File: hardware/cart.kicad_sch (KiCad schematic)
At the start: 4 parts, among them P1 MD-CART-FINGERS

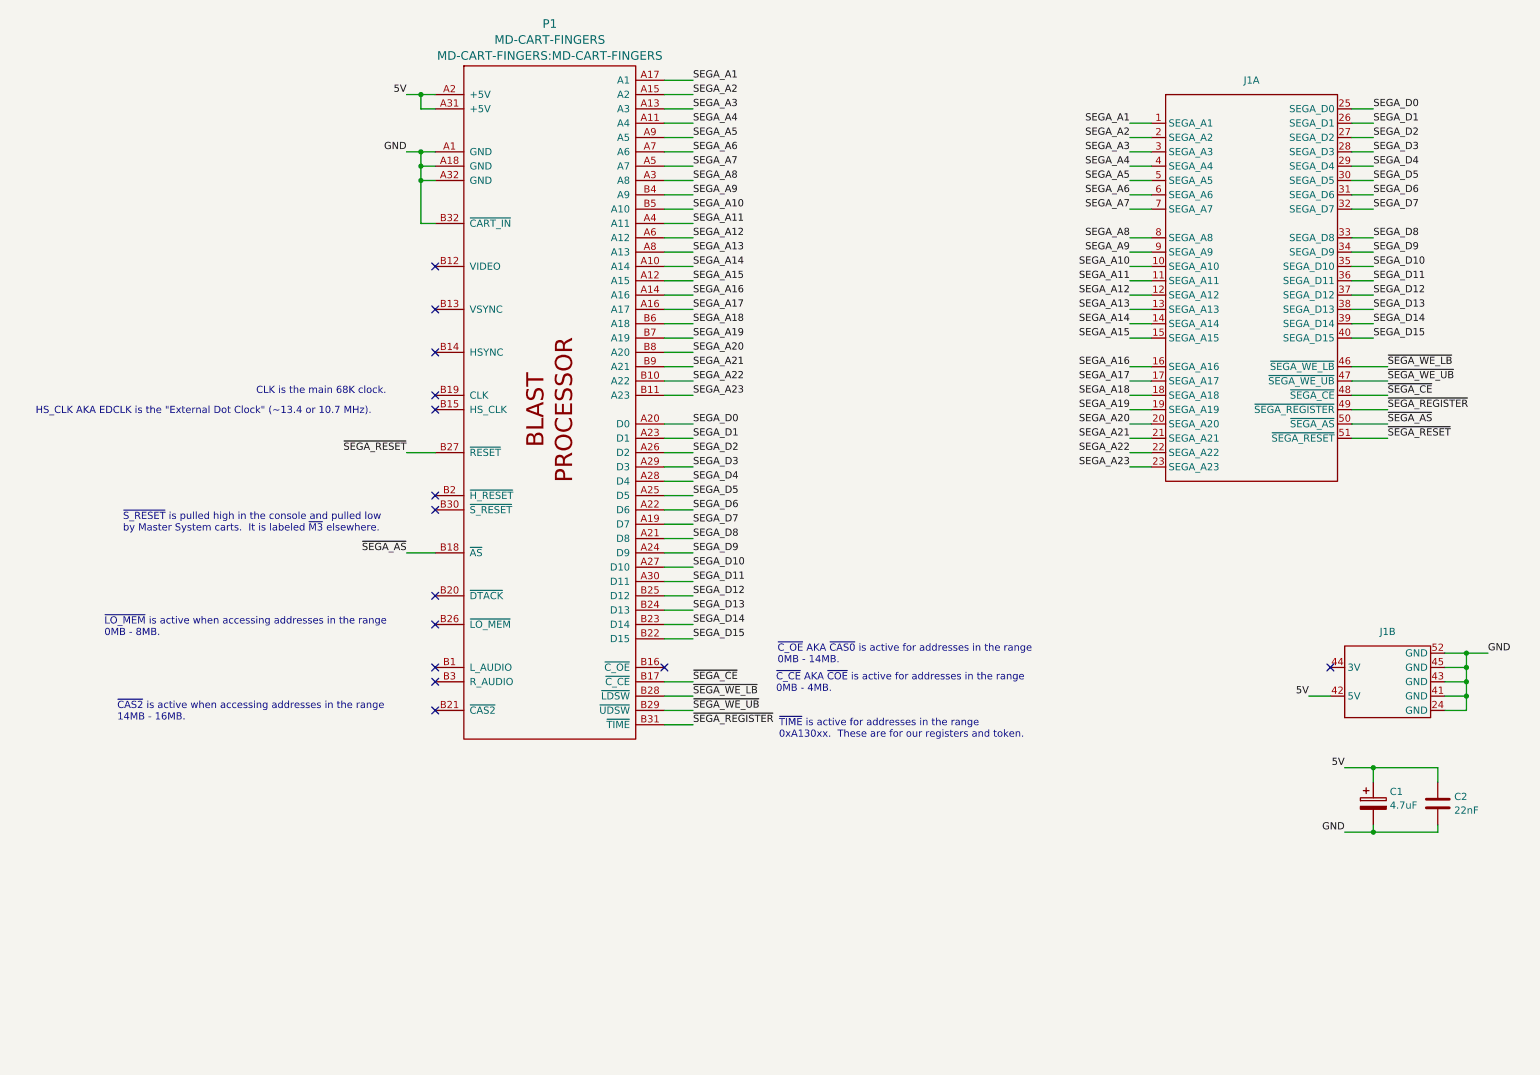
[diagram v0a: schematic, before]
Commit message: Massively reorganize board designs
Now planning to have most assembly done by JLCPCB, so trace sizes,
part selections, etc. are set accordingly.

New boards are:
 - cartridge interface & flash
 - microcontroller & registers
 - sram x2
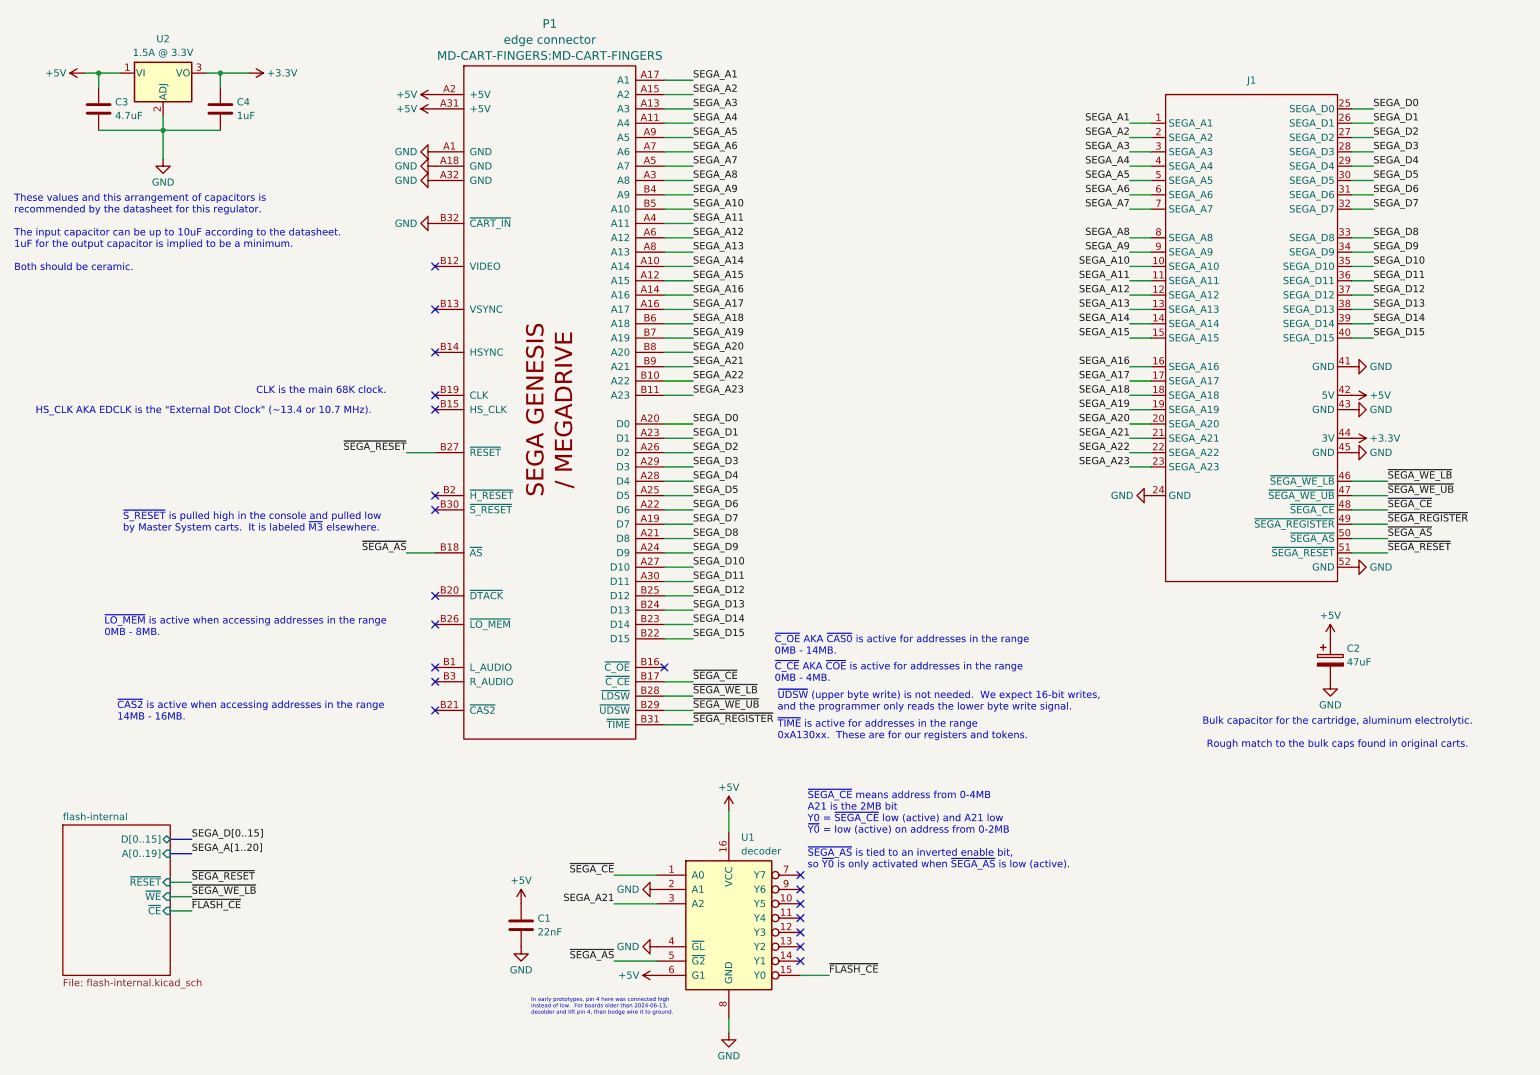
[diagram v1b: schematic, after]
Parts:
- removed C2: 22nF, Capacitor_SMD:C_1206_3216Metric_Pad1.33x1.80mm_HandSolder, symbol Device:C
- removed J1: ~, kinetoscope-cart-header:kinetoscope-cart-header-half, symbol kinetoscope-cart-header:kinetoscope-cart-header-half
- added C1: 22nF, Capacitor_SMD:C_0603_1608Metric, symbol Device:C
- added C3: 4.7uF, Capacitor_SMD:C_0603_1608Metric, symbol Device:C
- added C4: 1uF, Capacitor_SMD:C_0603_1608Metric, symbol Device:C
- added J1: ~, Connector_PinHeader_2.54mm:PinHeader_2x26_P2.54mm_Vertical, symbol kinetoscope-cart-header:kinetoscope-cart-header-a
- added U1: decoder, Package_SO:SO-16_3.9x9.9mm_P1.27mm, symbol 74xx:74LS137
- added U2: 1.5A @ 3.3V, Package_TO_SOT_THT:TO-220-3_Horizontal_TabDown, symbol Regulator_Linear:LM317_TO39
- C2: renamed from C1; value 4.7uF -> 47uF; Mouser Part Number (none) -> 710-860010372004; Part Number (none) -> 860010372004
- P1: value MD-CART-FINGERS -> edge connector; now left out of the parts list
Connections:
- net GND: now also C1.2, C3.2, C4.2, J1.24 (GND), J1.41 (GND), J1.43 (GND), J1.45 (GND), J1.52 (GND), U1.2 (A1), U1.4 (~{GL}), U1.8 (GND), U2.2 (ADJ)
- net SEGA_A1: now also J1.1 (SEGA_A1)
- net SEGA_A10: now also J1.10 (SEGA_A10)
- net SEGA_A11: now also J1.11 (SEGA_A11)
- net SEGA_A12: now also J1.12 (SEGA_A12)
- net SEGA_A13: now also J1.13 (SEGA_A13)
- net SEGA_A14: now also J1.14 (SEGA_A14)
- net SEGA_A15: now also J1.15 (SEGA_A15)
- net SEGA_A16: now also J1.16 (SEGA_A16)
- net SEGA_A17: now also J1.17 (SEGA_A17)
- net SEGA_A18: now also J1.18 (SEGA_A18)
- net SEGA_A19: now also J1.19 (SEGA_A19)
- net SEGA_A2: now also J1.2 (SEGA_A2)
- net SEGA_A20: now also J1.20 (SEGA_A20)
- net SEGA_A21: now also J1.21 (SEGA_A21), U1.3 (A2)
- net SEGA_A22: now also J1.22 (SEGA_A22)
- net SEGA_A23: now also J1.23 (SEGA_A23)
- net SEGA_A3: now also J1.3 (SEGA_A3)
- net SEGA_A4: now also J1.4 (SEGA_A4)
- net SEGA_A5: now also J1.5 (SEGA_A5)
- net SEGA_A6: now also J1.6 (SEGA_A6)
- net SEGA_A7: now also J1.7 (SEGA_A7)
- net SEGA_A8: now also J1.8 (SEGA_A8)
- net SEGA_A9: now also J1.9 (SEGA_A9)
- net SEGA_D0: now also J1.25 (SEGA_D0)
- net SEGA_D1: now also J1.26 (SEGA_D1)
- net SEGA_D10: now also J1.35 (SEGA_D10)
- net SEGA_D11: now also J1.36 (SEGA_D11)
- net SEGA_D12: now also J1.37 (SEGA_D12)
- net SEGA_D13: now also J1.38 (SEGA_D13)
- net SEGA_D14: now also J1.39 (SEGA_D14)
- net SEGA_D15: now also J1.40 (SEGA_D15)
- net SEGA_D2: now also J1.27 (SEGA_D2)
- net SEGA_D3: now also J1.28 (SEGA_D3)
- net SEGA_D4: now also J1.29 (SEGA_D4)
- net SEGA_D5: now also J1.30 (SEGA_D5)
- net SEGA_D6: now also J1.31 (SEGA_D6)
- net SEGA_D7: now also J1.32 (SEGA_D7)
- net SEGA_D8: now also J1.33 (SEGA_D8)
- net SEGA_D9: now also J1.34 (SEGA_D9)
- net ~{SEGA_AS}: now also J1.50 (~{SEGA_AS}), U1.5 (~{G2})
- net ~{SEGA_CE}: now also J1.48 (~{SEGA_CE}), U1.1 (A0)
- net ~{SEGA_REGISTER}: now also J1.49 (~{SEGA_REGISTER})
- net ~{SEGA_RESET}: now also J1.51 (~{SEGA_RESET})
- net ~{SEGA_WE_LB}: now also J1.46 (~{SEGA_WE_LB})
- net ~{SEGA_WE_UB}: now also J1.47 (~{SEGA_WE_UB})
- net 5V renamed +5V
- net +5V: now also C1.1, C3.1, J1.42 (5V), U1.16 (VCC), U1.6 (G1), U2.1 (VI)
- new net +3.3V: C4.1, J1.44 (3V), U2.3 (VO)
- new net ~{FLASH_CE}: U1.15 (Y0)
- no-connect marks 14 -> 20
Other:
- added sheet flash-internal (flash-internal.kicad_sch)
- note added: "Bulk capacitor for the cartridge, aluminum electrolytic. Rough match to the bulk caps found in original carts."
- note added: "In early prototypes, pin 4 here was connected high instead of low. For boards older than 2024-06-13, desolder and lift pin 4, then bodge wire it to ground."
- note added: "These values and this arrangement of capacitors is recommended by the datasheet for this regulator. The input capacitor can be up to 10uF according to the datasheet. 1uF for the output capacitor is implied to be a minimum. Both should be ceramic."
- note added: "~{SEGA_CE} means address from 0-4MB A21 is the 2MB bit Y0 = ~{SEGA_CE} low (active) and A21 low ~{Y0} = low (active) on address from 0-2MB ~{SEGA_AS} is tied to an inverted enable bit, so ~{Y0} is only activated when ~{SEGA_AS} is low (active)."
- note added: "~{TIME} is active for addresses in the range 0xA130xx. These are for our registers and tokens."
- note added: "~{UDSW} (upper byte write) is not needed. We expect 16-bit writes, and the programmer only reads the lower byte write signal."
- note removed: "~{TIME} is active for addresses in the range 0xA130xx. These are for our registers and token."
- moved on the sheet: C2

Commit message: Redo cart board
The first cartridge board I ordered did not work.  💰🚽

Problems I ran into:
 - The FlashKit Programmer sends 3.3V logic, not 5V logic like the
   Sega
 - I had one hard-coded input to my address decoder inverted
 - One pair of level translators had their supply voltages backward
 - I had hard-coded #OE on the flash chip, but #OE and #WE are
   mutually exclusive on this particular chip

Changes:
 - Add debug connectors (not populated by default) for power and flash
   control signals
 - Fix flash ~OE signal, which is mutually exclusive with ~WE
 - Fix level translators for compatibility with both 3.3V and 5V logic
 - Replace decoder with a smaller, simpler one with no latches and
   5V-tolerance
 - Reorient translators to simplify traces
 - Increase trace width for supply traces
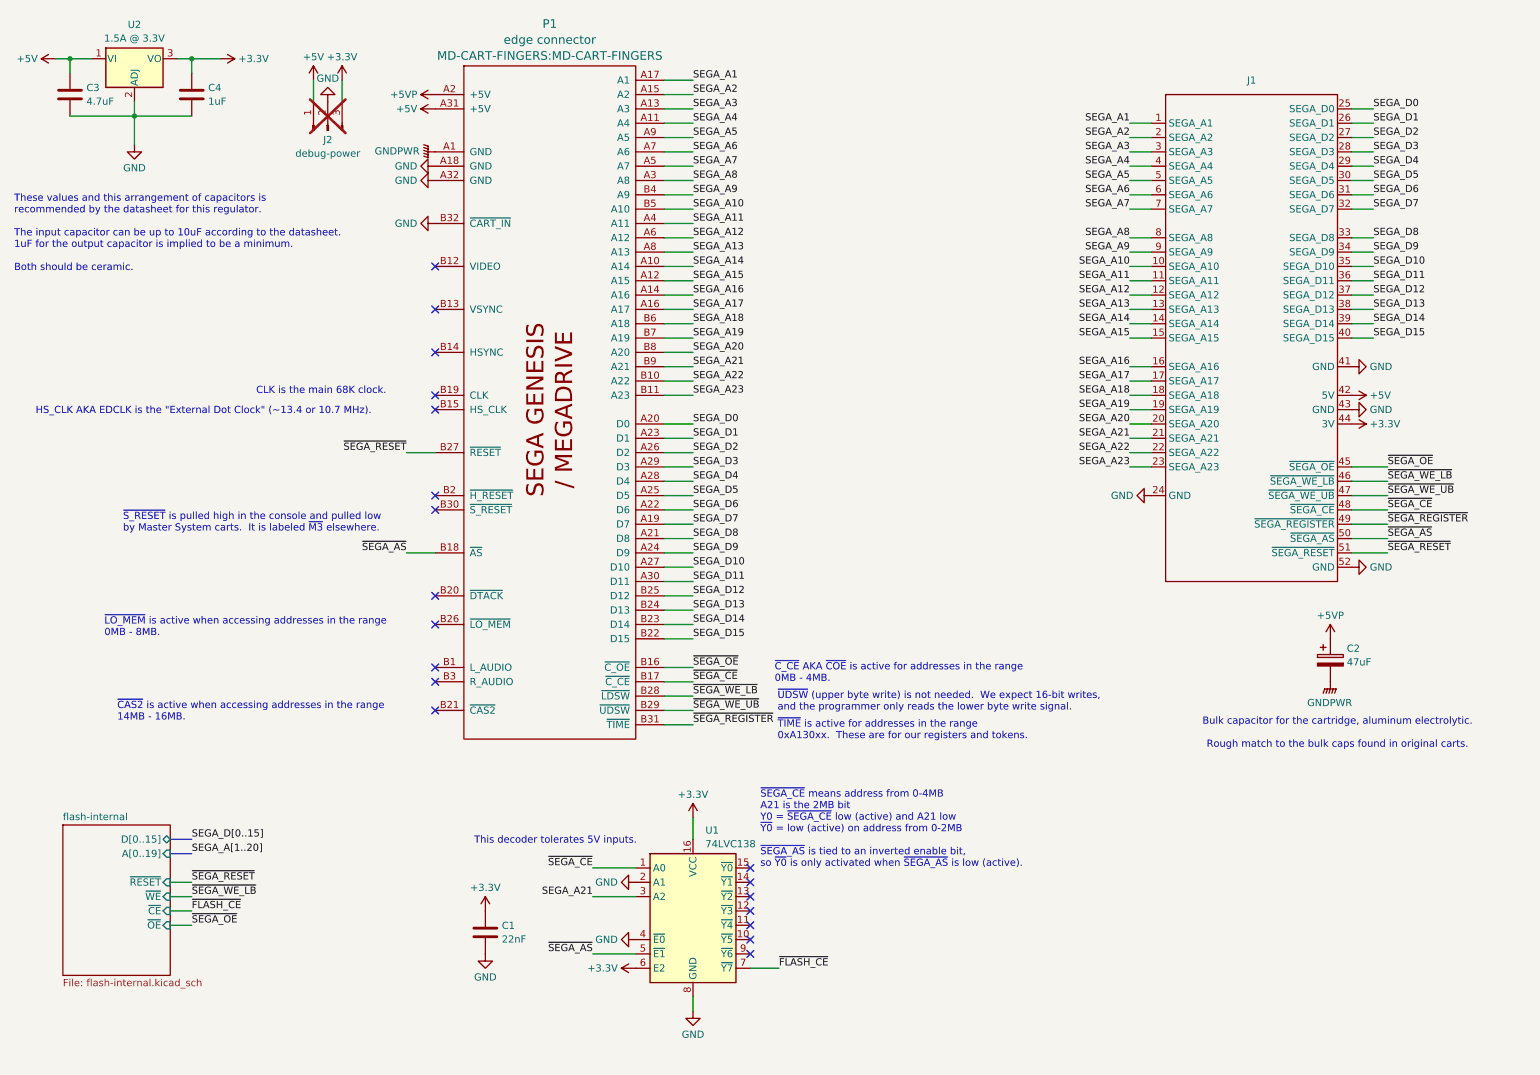
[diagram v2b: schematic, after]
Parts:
- removed U1: decoder, Package_SO:SO-16_3.9x9.9mm_P1.27mm, symbol 74xx:74LS137
- added J2: debug-power, Connector_PinHeader_2.54mm:PinHeader_1x03_P2.54mm_Horizontal, symbol Connector:Conn_01x03_Pin
- added U1: 74LVC138, Package_SO:SSOP-16_5.3x6.2mm_P0.65mm, symbol 74xx:74HC138
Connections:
- net +3.3V: now also C1.1, J2.3 (Pin_3), U1.16 (VCC), U1.6 (E2)
- net +5V: now also J2.1 (Pin_1); no longer C1.1, C2.1, P1.A2 (+5V)
- net GND: now also J2.2 (Pin_2), U1.2 (A1), U1.4 (~{E0}), U1.8 (GND); no longer C2.2, J1.45 (GND), P1.A1 (GND)
- net SEGA_A21: now also U1.3 (A2)
- net ~{FLASH_CE}: now also U1.7 (~{Y7})
- net ~{SEGA_AS}: now also U1.5 (~{E1})
- net ~{SEGA_CE}: now also U1.1 (A0)
- net ~{SEGA_OE}: now reaches P1.B16 (~{C_OE})
- net ~{SEGA_OE}: now also J1.45 (~{SEGA_OE})
- new net +5VP: C2.1, P1.A2 (+5V)
- new net GNDPWR: C2.2, P1.A1 (GND)
- no-connect marks 20 -> 19
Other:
- sheet flash-internal ports: added ~{OE}; removed none
- note added: "This decoder tolerates 5V inputs."
- note removed: "In early prototypes, pin 4 here was connected high instead of low. For boards older than 2024-06-13, desolder and lift pin 4, then bodge wire it to ground."
- note removed: "~{C_OE} AKA ~{CAS0} is active for addresses in the range 0MB - 14MB."
- moved on the sheet: C1, C3, C4, U2

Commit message: Fix footprint of new address decoder on cart board
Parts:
- U1: footprint Package_SO:SSOP-16_5.3x6.2mm_P0.65mm -> Package_SO:TSSOP-16_4.4x5mm_P0.65mm
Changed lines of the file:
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@@
 			)
 		)
-		(property "Footprint" "Package_SO:SSOP-16_5.3x6.2mm_P0.65mm"
+		(property "Footprint" "Package_SO:TSSOP-16_4.4x5mm_P0.65mm"
 			(at 133.35 173.99 0)
 			(effects
